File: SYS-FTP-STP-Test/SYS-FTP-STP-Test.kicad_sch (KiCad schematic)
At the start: 5 parts

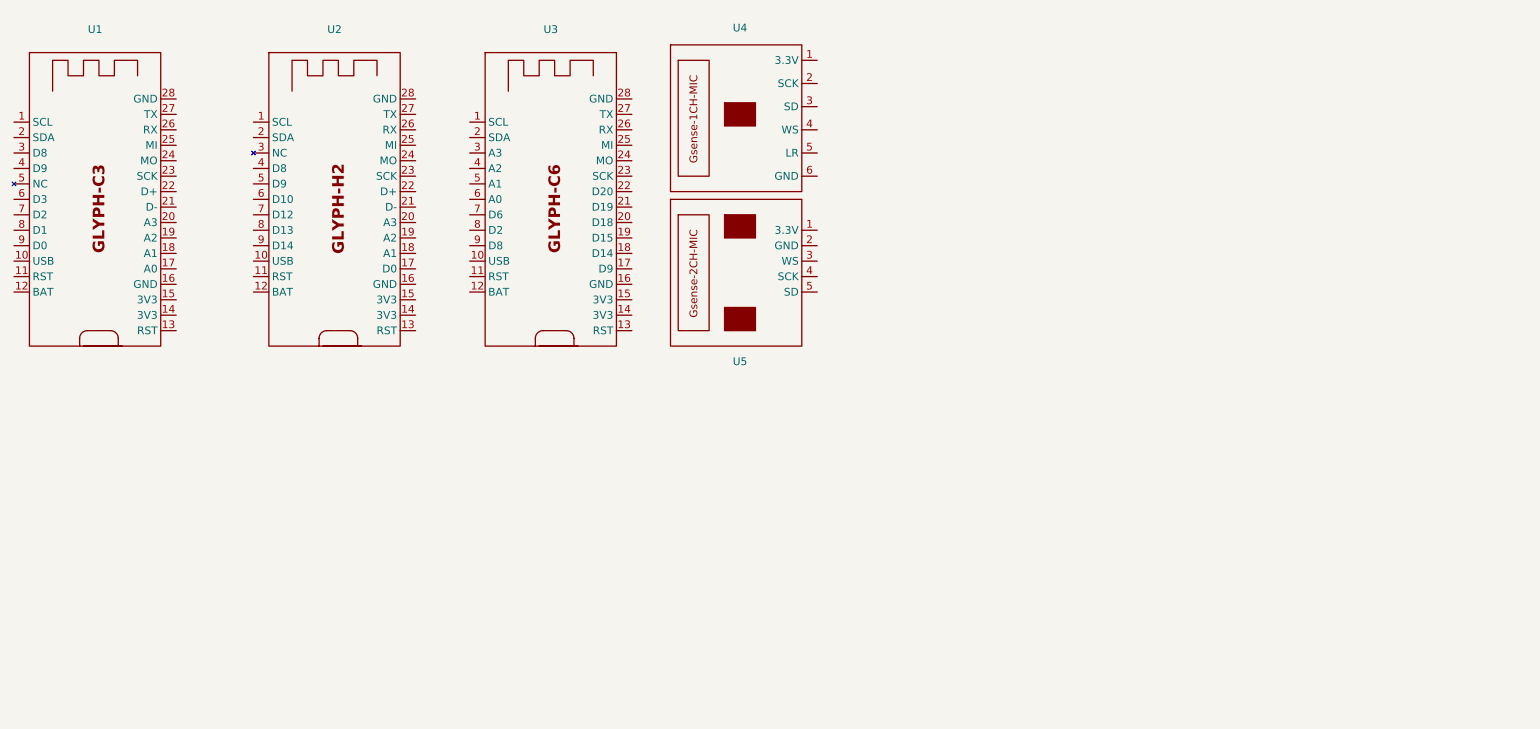
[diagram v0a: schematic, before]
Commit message: Symbols added
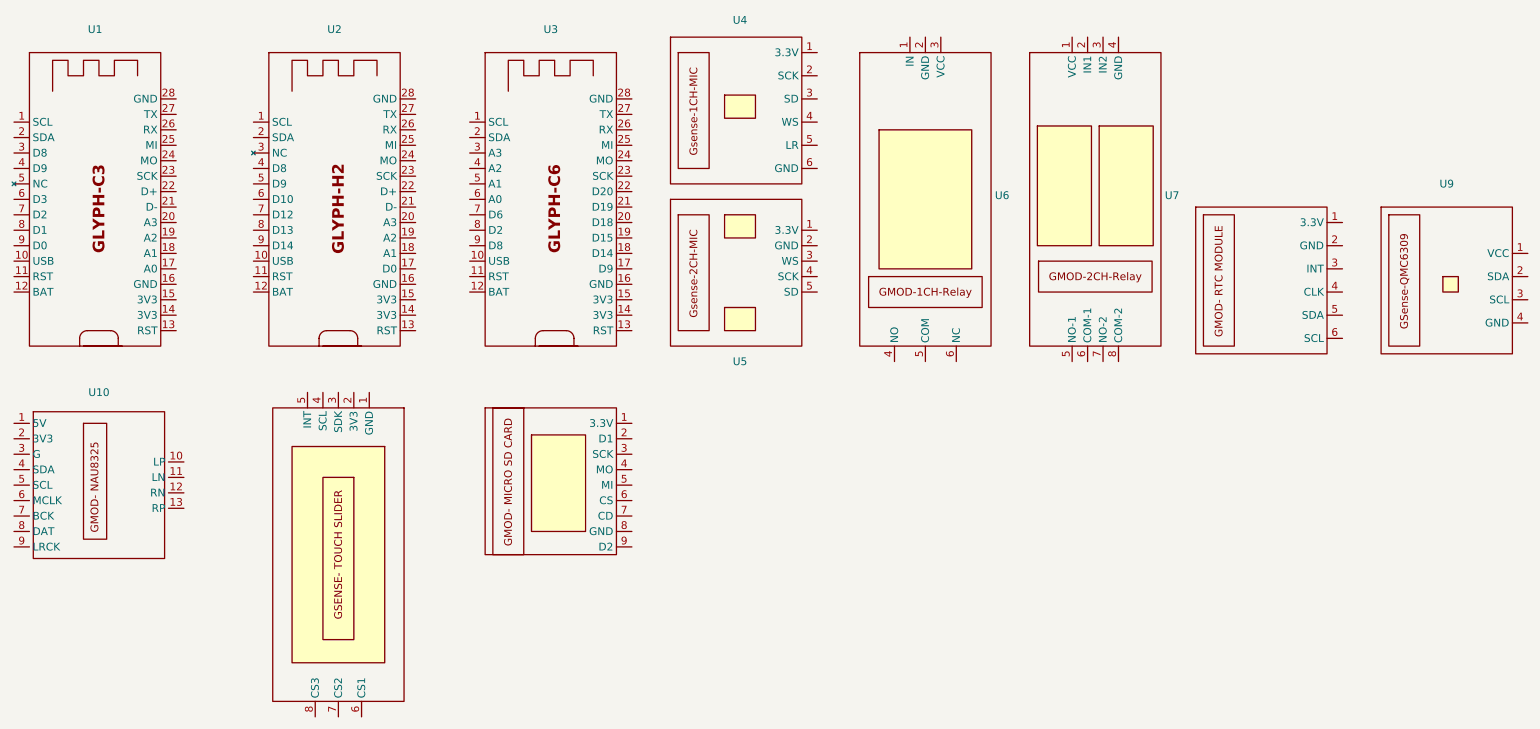
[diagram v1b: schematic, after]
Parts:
- added U10: ~, Audiocodec_foot:Audio_codec, symbol Audiocodec_symbol:GMOD-NAU8325
- added U11: ~, symbol Touch Slider:GSENSE-_Touch_Slider
- added U12: ~, symbol SD SYMBOL:GMOD- MICRO SD CARD
- added U6: ~, Ch1_Relay_footprint:CH1_Relay_foot, symbol Relay_ch1_symbol:GMOD-1CH-Relay
- added U7: ~, Relay_CH2_footprint:Relay_CH2, symbol Relay_CH2_symbol:GMOD-CH2-Relay
- added U8: ~, symbol RTC_module_symbol:GMOD-RTC_Module
- added U9: ~, symbol Magnetometer_sym:Gsense-Magnetometer
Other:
- moved on the sheet: U4
